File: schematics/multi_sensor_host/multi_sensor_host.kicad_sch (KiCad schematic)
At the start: 0 parts

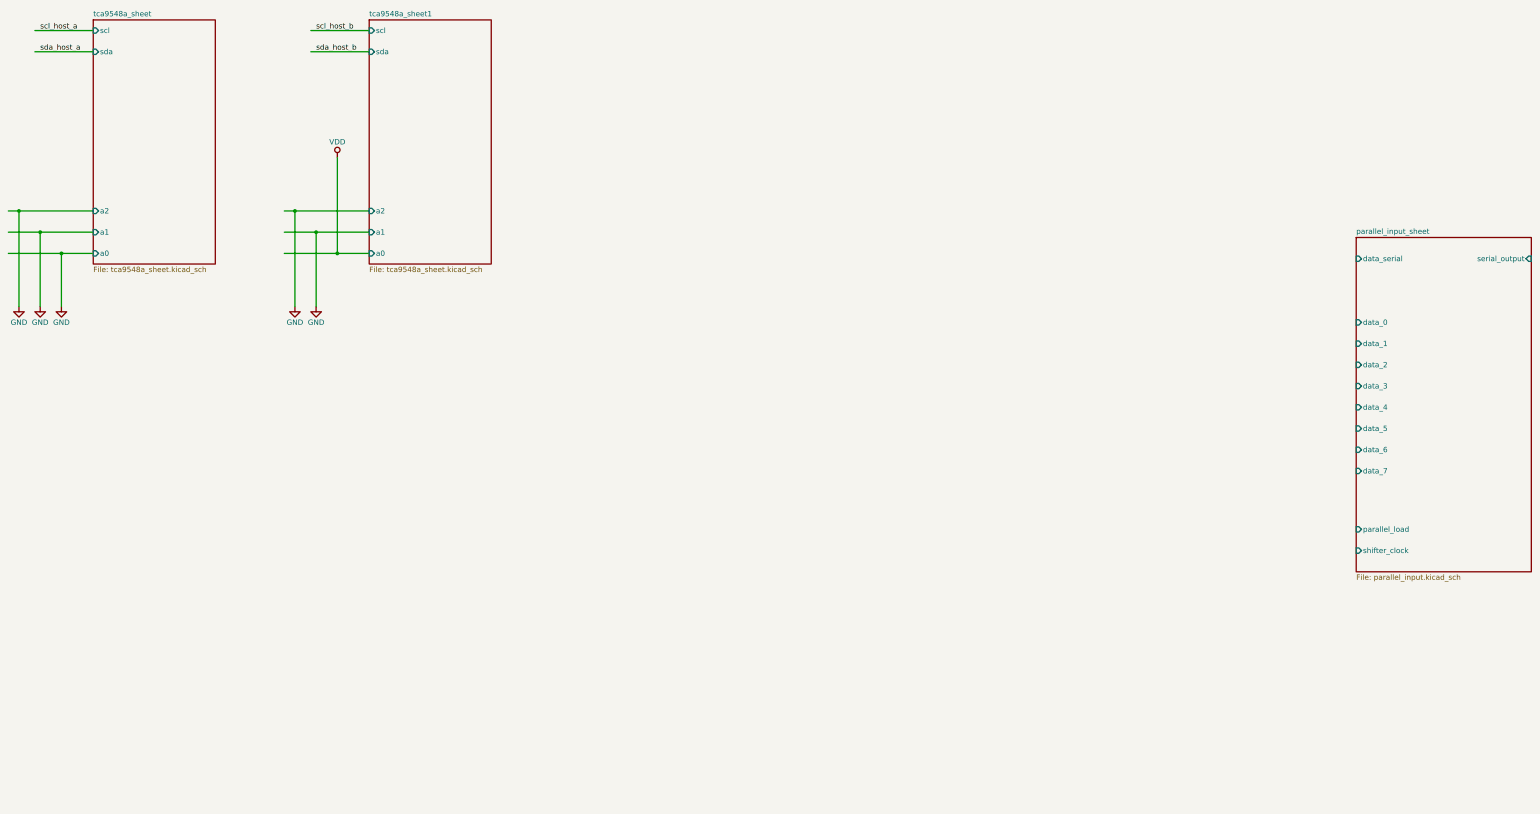
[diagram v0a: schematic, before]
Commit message: 4 shift registers are added.
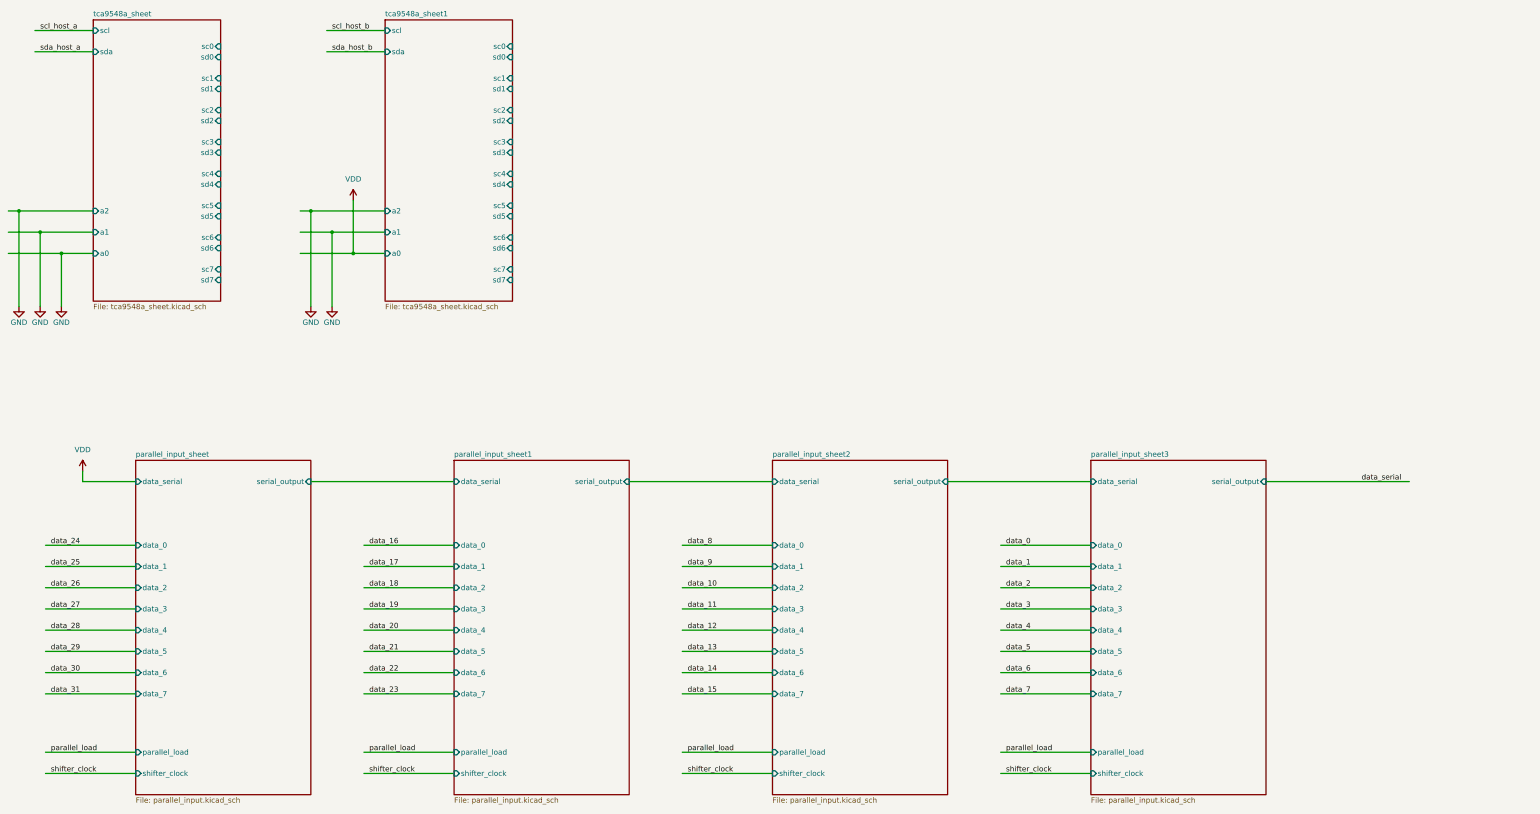
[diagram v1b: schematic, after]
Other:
- added sheet parallel_input_sheet1 (parallel_input.kicad_sch)
- added sheet parallel_input_sheet2 (parallel_input.kicad_sch)
- added sheet parallel_input_sheet3 (parallel_input.kicad_sch)
- sheet tca9548a_sheet ports: added sc0, sc1, sc2, sc3, sc4, sc5, sc6, sc7, sd0, sd1, sd2, sd3, sd4, sd5, sd6, sd7; removed none
- sheet tca9548a_sheet1 ports: added sc0, sc1, sc2, sc3, sc4, sc5, sc6, sc7, sd0, sd1, sd2, sd3, sd4, sd5, sd6, sd7; removed none

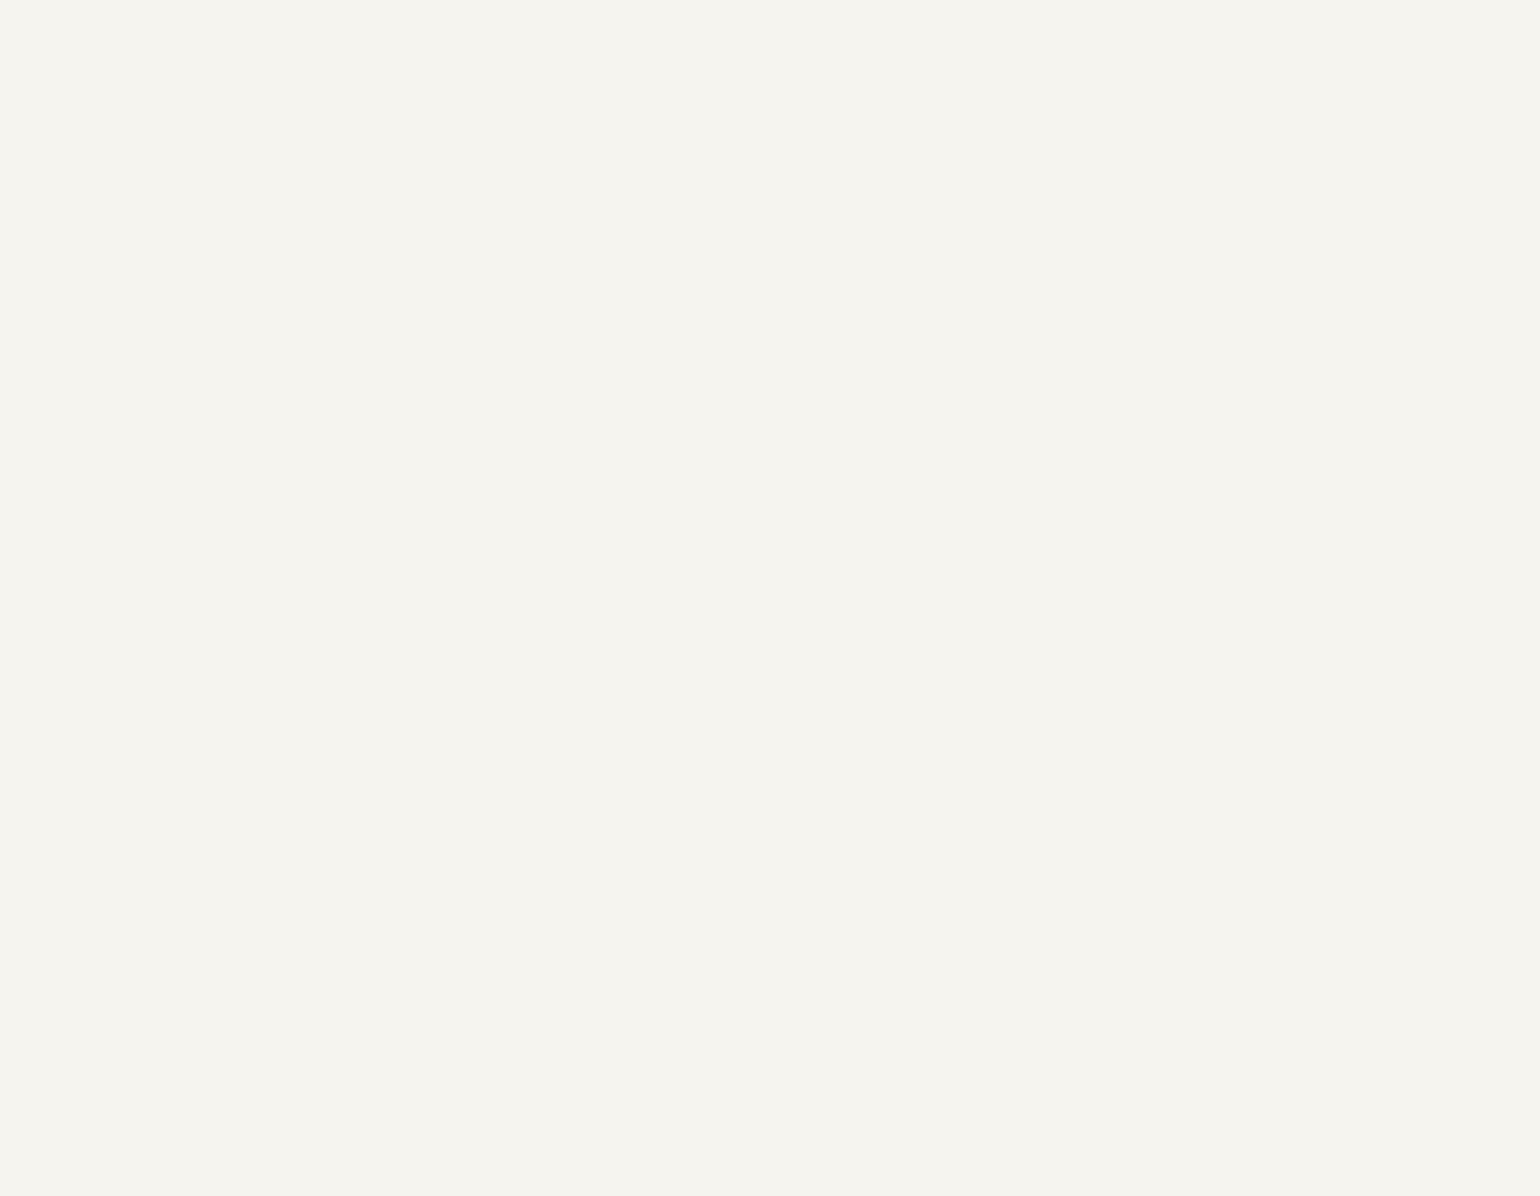
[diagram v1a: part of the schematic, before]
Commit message: Added battery charger.
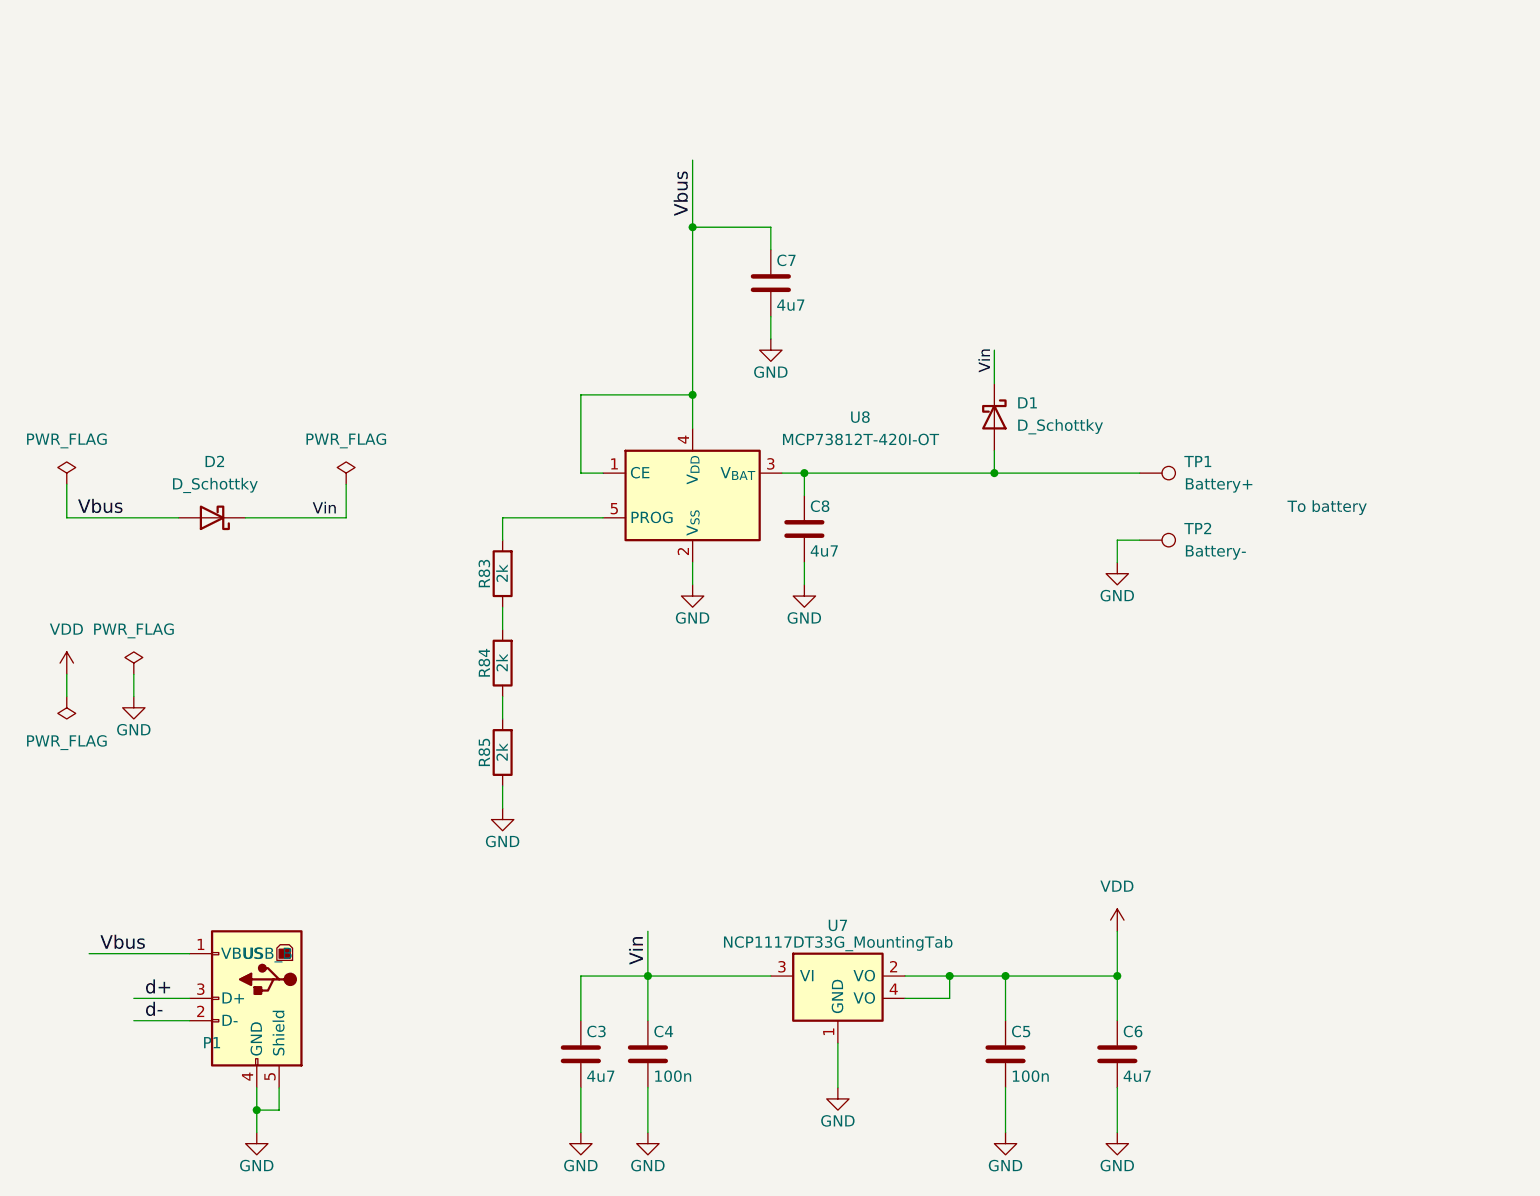
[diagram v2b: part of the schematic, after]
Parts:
- added C3, C6, C7, C8: 4u7, Capacitors_SMD:C_0603, symbol multi_i2c-rescue:C
- added C4, C5: 100n, Capacitors_SMD:C_0603, symbol multi_i2c-rescue:C
- added D1, D2: D_Schottky, symbol Device:D_Schottky
- added P1: USB_B, Connectors:USB_B, symbol multi_i2c-rescue:USB_B
- added R83, R84, R85: 2k, Resistors_SMD:R_0603, symbol multi_i2c-rescue:R
- added TP1: Battery+, symbol Connector:TestPoint
- added TP2: Battery-, symbol Connector:TestPoint
- added U7: NCP1117DT33G_MountingTab, TO_SOT_Packages_SMD:SOT-223, symbol multi_i2c-rescue:NCP1117DT33G_MountingTab
- added U8: MCP73812T-420I-OT, Package_TO_SOT_SMD:SOT-23-5, symbol Battery_Management:MCP73812T-420I-OT
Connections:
- net GND: now also C3.2, C4.2, C5.2, C6.2, C7.2, C8.2, P1.4 (GND), P1.5 (Shield), R85.1, TP2.1, U7.1 (GND), U8.2 (V_{SS})
- net VDD: now also C5.1, C6.1, U7.2 (VO), U7.4 (VO)
- new net: C8.1, D1.2 (A), TP1.1, U8.3 (V_{BAT})
- new net: R84.1, R85.2
- new net: R83.1, R84.2
- new net: R83.2, U8.5 (PROG)
- new net Vbus: C7.1, D2.2 (A), P1.1 (VBUS), U8.1 (CE), U8.4 (V_{DD})
- new net Vin: C3.1, C4.1, D1.1 (K), D2.1 (K), U7.3 (VI)
- new net d+: P1.3 (D+)
- new net d-: P1.2 (D-)
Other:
- note added: "To battery"

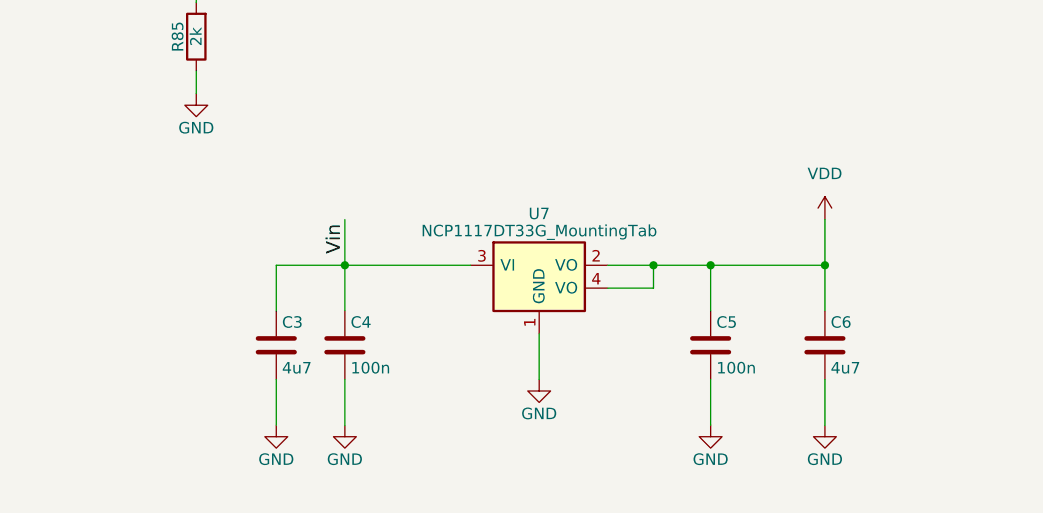
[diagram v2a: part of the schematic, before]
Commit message: Replaced linear regulator with fixed 3.3V Buck converter MCP1603.
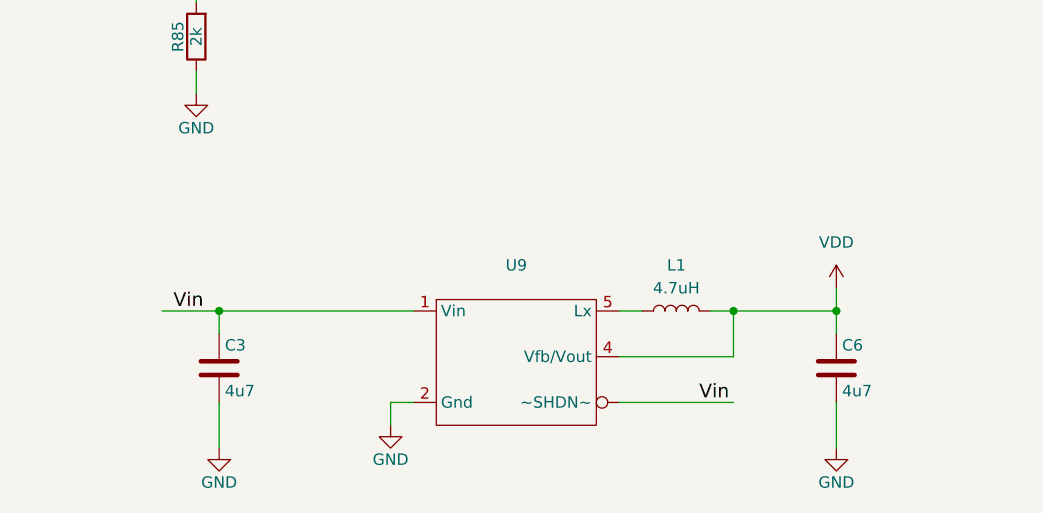
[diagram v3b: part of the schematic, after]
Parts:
- removed C4, C5: 100n, Capacitors_SMD:C_0603, symbol multi_i2c-rescue:C
- removed U7: NCP1117DT33G_MountingTab, TO_SOT_Packages_SMD:SOT-223, symbol multi_i2c-rescue:NCP1117DT33G_MountingTab
- added L1: 4.7uH, symbol Device:L
- added U9: ~, Package_TO_SOT_SMD:SOT-23-5_HandSoldering, symbol mcp1603:MCP1603T-330I/OS
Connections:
- net GND: now also U9.2 (Gnd)
- net VDD: now also L1.2, U9.4 (Vfb/Vout)
- net Vin: now also U9. (~SHDN~), U9.1 (Vin)
- new net: L1.1, U9.5 (Lx)
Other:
- moved on the sheet: C3, C6

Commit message: Inserted ESP-12S WIFI module.
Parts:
- added J1: esp_rst, symbol Connector:Conn_01x02_Pin
- added J2: esp_flash_wifi, symbol Connector:Conn_01x02_Pin
- added J3: esp_flash_uart, symbol Connector:Conn_01x02_Pin
- added J4: Conn_01x04_Pin, symbol Connector:Conn_01x04_Pin
- added R86: 10k, Resistors_SMD:R_0603, symbol multi_i2c-rescue:R
- added U7: ~, esp-12s:ESP-12S, symbol esp_12s:ESP-12S
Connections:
- net GND: now also J1.2 (Pin_2), J3.2 (Pin_2), J4.2 (Pin_2), U7.9 (GND)
- net VDD: now also J2.1 (Pin_1), J4.1 (Pin_1), R86.1, U7.8 (VCC_3.3V)
- new net: J3.1 (Pin_1), U7.12 (IO_0)
- new net: J1.1 (Pin_1), U7.1 (RST)
- new net: J2.2 (Pin_2), U7.10 (IO_15/MTDO/SPI_CS/UART0_RTS)
- new net eps_tx: J4.3 (Pin_3), U7.16 (IO_1/UART0_TX)
- new net esp_i2c_scl: U7.5 (IO_14/SPI_CLK/IR_T/I2C_SCL)
- new net esp_i2c_sda: U7.11 (IO_2/UART1_TXD/I2C_SDA)
- new net esp_rx: J4.4 (Pin_4), R86.2, U7.15 (IO_3/UART0_RX/SPI_CS)
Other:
- note added: "ESP-12S doesn't have pullup inside the module."
- moved on the sheet: C3, C6, C7, C8, D1, D2, L1, P1, R83, R84, R85, TP1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

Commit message: Added stm32f405rgt6.
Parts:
- added C10: 4u7, Capacitor_SMD:C_0603_1608Metric, symbol bridge-rescue:C
- added C23, C24, C27, C30, C31, C5: 100n, Capacitor_SMD:C_0603_1608Metric, symbol bridge-rescue:C
- added C28, C29: 2u2, Capacitor_SMD:C_0603_1608Metric, symbol bridge-rescue:C
- added C4, C9: 18p, Capacitor_SMD:C_0603_1608Metric, symbol bridge-rescue:C
- added D3, D4: LED, LED_THT:LED_D3.0mm, symbol bridge-rescue:LED
- added J6: MY_USB_B, Connector_USB:USB_B_Horizontal, symbol bridge-rescue:MY_USB_B
- added J7: swd, Connector_PinHeader_1.27mm:PinHeader_1x03_P1.27mm_Vertical, symbol bridge-rescue:CONN_01X03
- added P2: ~rst~, Connector_PinHeader_1.27mm:PinHeader_1x02_P1.27mm_Vertical, symbol bridge-rescue:CONN_01X02
- added P3: bootldr, Connector_PinHeader_1.27mm:PinHeader_1x02_P1.27mm_Vertical, symbol bridge-rescue:CONN_01X02
- added R87, R88: 10k 5%, Resistor_SMD:R_0603_1608Metric, symbol bridge-rescue:R
- added R89, R90: 1k 5%, Resistor_SMD:R_0603_1608Metric, symbol bridge-rescue:R
- added R91: 100 5%, Resistor_SMD:R_0603_1608Metric, symbol bridge-rescue:R
- added U11: stm32f405rgt6, symbol bridge-rescue:stm32f405rgt6
- added Y1: Crystal, symbol Device:Crystal
- J4: value Conn_01x04_Pin -> esp_flash_port
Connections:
- net GND: now also C10.2, C23.2, C24.2, C27.2, C28.1, C29.1, C30.2, C31.2, C4.1, C5.2, C9.2, D3.2 (A), D4.2 (A), J6.4 (GND), J6.5 (Shield), J7.2 (P2), P2.2 (P2), R87.1, U11.12 (VssA), U11.18 (Vss_1), U11.63 (Vss_2)
- net VDD: now also C23.1, C24.1, C27.1, C30.1, C31.1, P3.1 (P1), R88.1, U11.1 (VBAT), U11.13 (VDDA), U11.19 (VDD_4), U11.32 (VDD_1), U11.48 (VDD_2), U11.64 (VDD_3)
- new net: D3.1 (K), R89.2
- new net: C9.1, R91.2, Y1.2
- new net: C28.2, U11.31 (Vcap_1)
- new net: C29.2, U11.47 (Vcap_2)
- new net: D4.1 (K), R90.2
- new net boot0: P3.2 (P2), R87.2, U11.60 (BOOT0)
- new net clk-in: C4.2, U11.5 (PD0_OSC_IN), Y1.1
- new net clk-out: R91.1, U11.6 (PD1_OSC_OUT)
- new net dev_dm: U11.44 (PA11___OTG_FS_DM)
- new net dev_dp: U11.45 (PA12___OTG_FS_DP)
- new net host_dm: J6.2 (D-), U11.35 (PB14___OTG_HS_DM)
- new net host_dp: J6.3 (D+), U11.36 (PB15___OTG_HS_DP)
- new net i2c_scl: U11.58 (PB6__USART1_TX)
- new net i2c_sda: U11.59 (PB7__USART1_RX)
- new net led-0: R89.1, U11.15 (PA1)
- new net led-1: R90.1, U11.16 (PA2)
- new net pa4: U11.20 (PA4)
- new net pa5: U11.21 (PA5)
- new net pa6: U11.22 (PA6)
- new net pa7: U11.23 (PA7)
- new net pb0: U11.26 (PB0)
- new net pb1: U11.27 (PB1)
- new net pb10: U11.29 (PB10___USART3_TX)
- new net pb11: U11.30 (PB11___USART3_RX)
- new net pb2: U11.28 (PB2)
- new net pc4: U11.24 (PC4)
- new net pc5: U11.25 (PC5)
- new net spi_miso: U11.52 (PC11__USART4_RX)
- new net spi_mosi: U11.53 (PC12)
- new net spi_nss: U11.50 (PA15___JTDI)
- new net spi_sck: U11.51 (PC10___USART4_TX)
- new net swd_clk: J7.1 (P1), U11.49 (PA14___JTCK-SWCLK)
- new net swd_io: J7.3 (P3), U11.46 (PA13___JTMS-SWDIO)
- new net vbus: C10.1, J6.1 (VBUS)
- new net ~{mcu-rst}: C5.1, P2.1 (P1), R88.2, U11.7 (NRST)
- no-connect marks 0 -> 24
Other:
- note added: "Low speed: 1.5 Mb/s Full speed: 12 Mb/s High speed: 480 Mb/s"
